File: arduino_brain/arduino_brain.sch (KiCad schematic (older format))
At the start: 57 parts, among them Q1 2N3904, Q10 2N3904, Q11 2N3906, Q2 TIP120, Q3 TIP120, Q4 2N3904, Q5 2N3906, Q6 2N3904, Q7 2N3906, Q8 2N3904, Q9 2N3906, U2 CRE1S2412SC

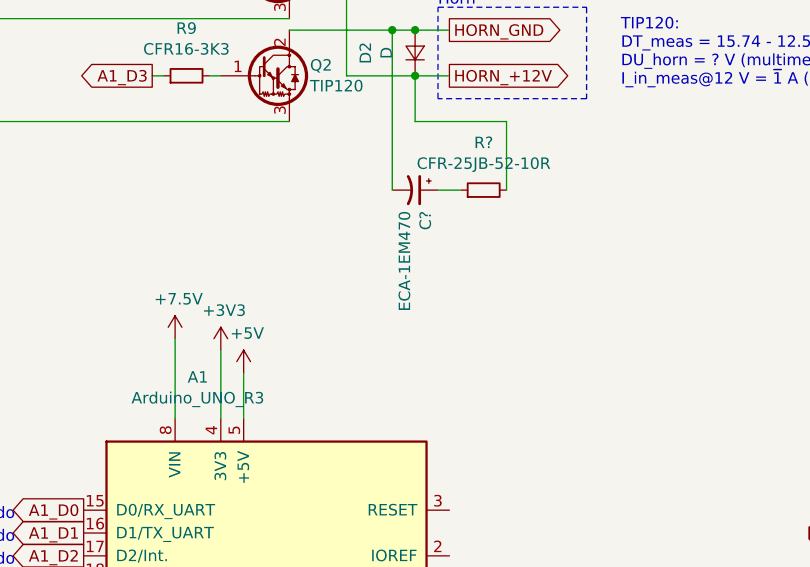
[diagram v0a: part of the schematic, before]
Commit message: Beefed up snubber capacitor
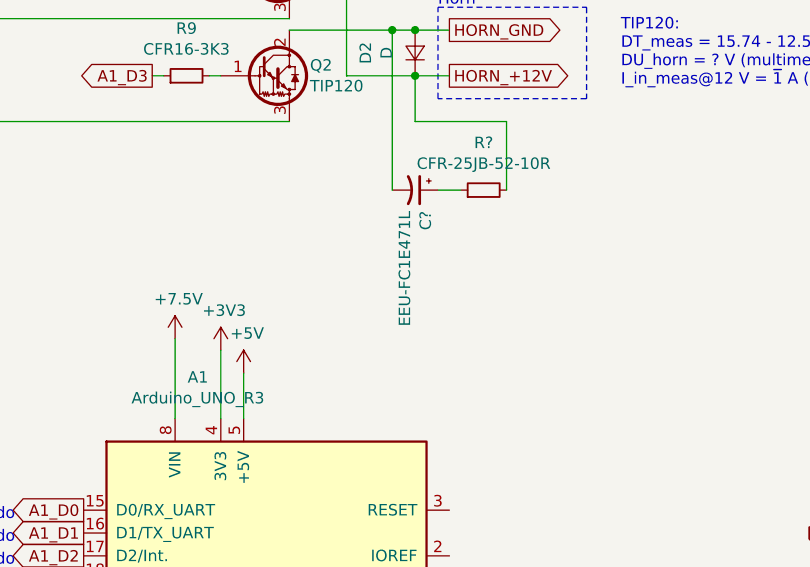
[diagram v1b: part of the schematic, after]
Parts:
- C?: value ECA-1EM470 -> EEU-FC1E471L
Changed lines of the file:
@@
 P 6850 5050
 F 0 "C?" H 6941 5096 50  0000 L CNN
-F 1 "ECA-1EM470" H 6941 5005 50  0000 L CNN
+F 1 "EEU-FC1E471L" H 6941 5005 50  0000 L CNN
 F 2 "" H 6850 5050 50  0001 C CNN
 F 3 "~" H 6850 5050 50  0001 C CNN

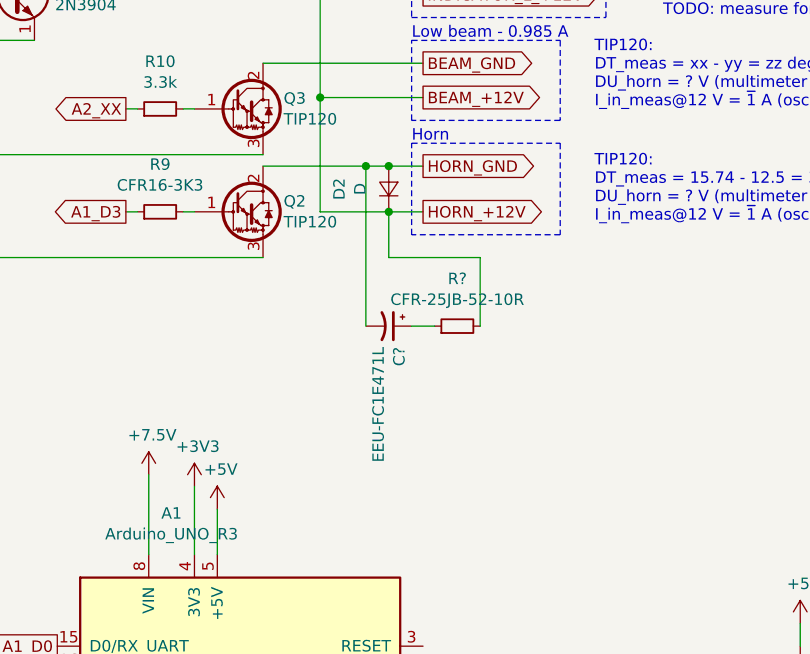
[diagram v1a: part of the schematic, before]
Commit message: Added cap on supply, removed snubber cap
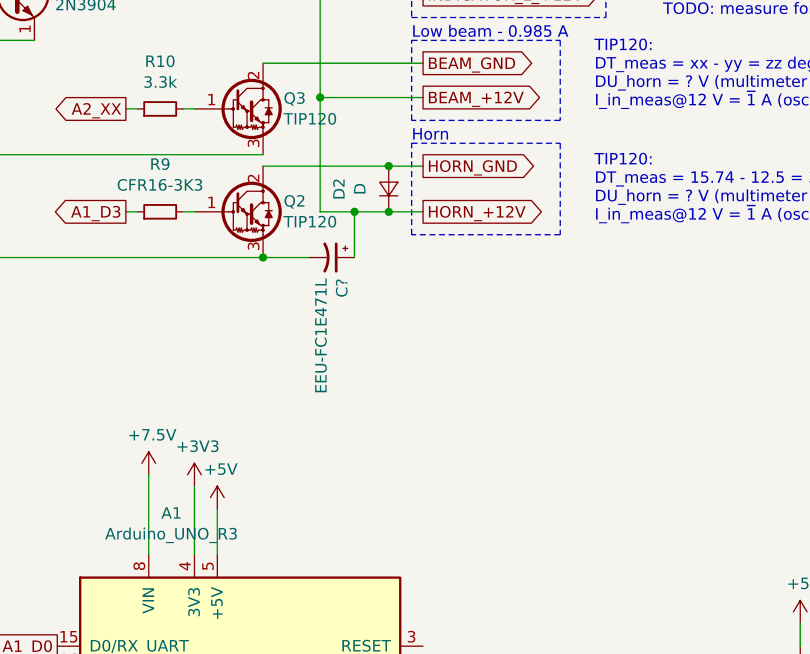
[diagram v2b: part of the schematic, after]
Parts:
- removed R?: CFR-25JB-52-10R, symbol Device:R_Small
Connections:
- net +12V: now also C?.1
- net -BATT: now also C?.2
- net HORN_GND: no longer C?.2
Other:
- moved on the sheet: C?
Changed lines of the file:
@@
 	8650 6350 8650 6450
 Wire Wire Line
-	6550 4550 6850 4550
+	6550 4550 6700 4550
 Wire Wire Line
 	6850 850  6850 2100
 $Comp
-L Device:R_Small R?
-U 1 1 5E512CDD
-P 7150 5050
-F 0 "R?" V 7357 5050 50  0000 C CNN
-F 1 "CFR-25JB-52-10R" V 7266 5050 50  0000 C CNN
-F 2 "" V 7080 5050 50  0001 C CNN
-F 3 "~" H 7150 5050 50  0001 C CNN
-	1    7150 5050
-	0    -1   -1   0
+L Device:CP1_Small C?
+U 1 1 5E54D93D
+P 6600 4750
+F 0 "C?" H 6691 4796 50  0000 L CNN
+F 1 "EEU-FC1E471L" H 6691 4705 50  0000 L CNN
+F 2 "" H 6600 4750 50  0001 C CNN
+F 3 "~" H 6600 4750 50  0001 C CNN
+	1    6600 4750
+	0    1    1    0
 $EndComp
 Wire Wire Line
-	6950 5050 7050 5050
+	6300 4350 6850 4350
 Wire Wire Line
-	6750 5050 6750 4350
+	6500 4750 6300 4750
+Connection ~ 6300 4750
 Wire Wire Line
-	6300 4350 6750 4350
-Connection ~ 6750 4350
+	6700 4750 6700 4550
+Connection ~ 6700 4550
 Wire Wire Line
-	6750 4350 6850 4350
-Wire Wire Line
-	7250 5050 7250 4750
-Wire Wire Line
-	7250 4750 6850 4750
-Wire Wire Line
-	6850 4750 6850 4550
-$Comp
-L Device:CP1_Small C?
-U 1 1 5E54D93D
-P 6850 5050
-F 0 "C?" H 6941 5096 50  0000 L CNN
-F 1 "EEU-FC1E471L" H 6941 5005 50  0000 L CNN
-F 2 "" H 6850 5050 50  0001 C CNN
-F 3 "~" H 6850 5050 50  0001 C CNN
-	1    6850 5050
-	0    1    1    0
-$EndComp
+	6700 4550 6850 4550
 $EndSCHEMATC

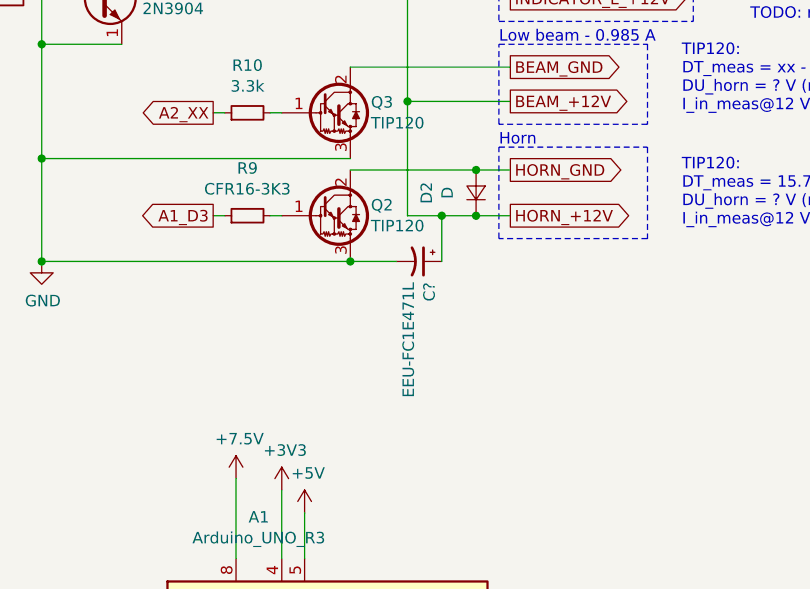
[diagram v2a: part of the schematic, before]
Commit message: Removed cap on supply
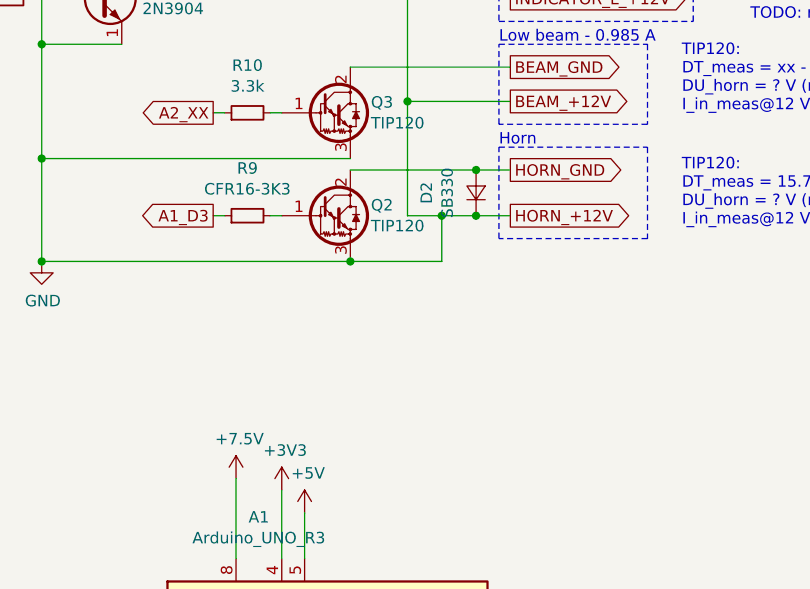
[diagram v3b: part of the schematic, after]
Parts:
- removed C?: EEU-FC1E471L, symbol Device:CP1_Small
- D2: value D -> SB330
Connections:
- net -BATT is gone; now on net +12V: A1.7 (GND), A2.7 (GND), C?.2, C?.2, C?.2, C?.2, C?.2, C?.2, C?.2, C?.2, D?.2 (A), Q10.1 (E), Q2.3 (E), Q3.3 (E), Q4.1 (E), Q6.1 (E), Q6.2 (B), Q8.1 (E), R14.2, R?.1, R?.2, R?.2, U2.1 (-VIN), U2.3 (-VOUT), U?.1 (GND), U?.3 (GND)
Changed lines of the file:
@@
 P 6850 4450
 F 0 "D2" H 6850 4666 50  0000 C CNN
-F 1 "D" H 6850 4575 50  0000 C CNN
+F 1 "SB330" H 6850 4575 50  0000 C CNN
 F 2 "" H 6850 4450 50  0001 C CNN
 F 3 "~" H 6850 4450 50  0001 C CNN
@@
 Wire Wire Line
 	6850 850  6850 2100
-$Comp
-L Device:CP1_Small C?
-U 1 1 5E54D93D
-P 6600 4750
-F 0 "C?" H 6691 4796 50  0000 L CNN
-F 1 "EEU-FC1E471L" H 6691 4705 50  0000 L CNN
-F 2 "" H 6600 4750 50  0001 C CNN
-F 3 "~" H 6600 4750 50  0001 C CNN
-	1    6600 4750
-	0    1    1    0
-$EndComp
 Wire Wire Line
 	6300 4350 6850 4350
-Wire Wire Line
-	6500 4750 6300 4750
 Connection ~ 6300 4750
 Wire Wire Line
@@
 Wire Wire Line
 	6700 4550 6850 4550
+Wire Wire Line
+	6300 4750 6700 4750
 $EndSCHEMATC

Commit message: Added capactitor between base and emitter of pnp transistor horn
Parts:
- added C?: 1C25X7R104K100B, symbol Device:C_Small
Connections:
- net +12V: now also C?.1
- net at Q5.2 (B), R12.2: now also C?.2
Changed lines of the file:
@@
 Wire Wire Line
 	6550 1150 6550 2000
-Wire Wire Line
-	6300 1150 5950 1150
 Connection ~ 6300 1150
 Wire Wire Line
@@
 Wire Wire Line
 	6300 4750 6700 4750
+$Comp
+L Device:C_Small C?
+U 1 1 5E598FF6
+P 6000 1300
+F 0 "C?" V 6229 1300 50  0000 C CNN
+F 1 "1C25X7R104K100B" V 6138 1300 50  0000 C CNN
+F 2 "" H 6000 1300 50  0001 C CNN
+F 3 "~" H 6000 1300 50  0001 C CNN
+	1    6000 1300
+	1    0    0    -1
+$EndComp
+Wire Wire Line
+	5950 1150 6000 1150
+Wire Wire Line
+	6000 1200 6000 1150
+Connection ~ 6000 1150
+Wire Wire Line
+	6000 1150 6300 1150
+Wire Wire Line
+	6000 1400 6000 1450
+Connection ~ 6000 1450
 $EndSCHEMATC

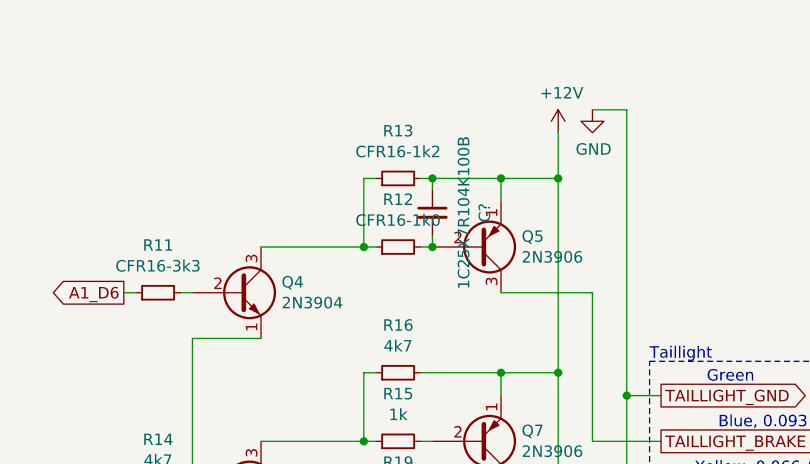
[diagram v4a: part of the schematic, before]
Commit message: Added capactitor in parallel to R2 (EE.SE), removed the previous cap
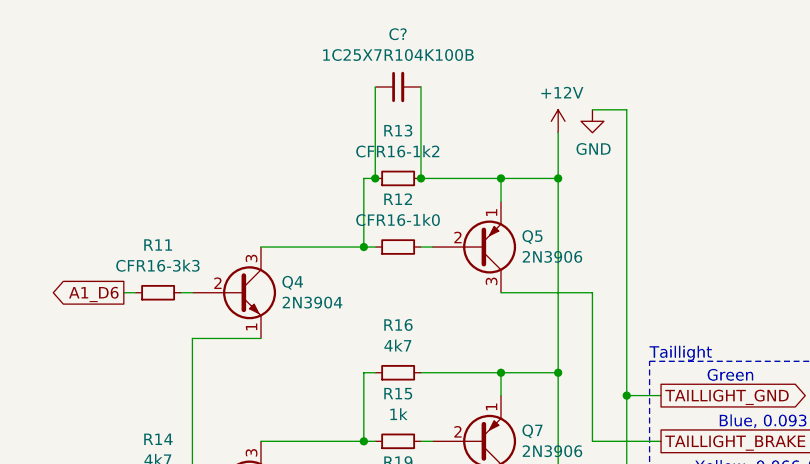
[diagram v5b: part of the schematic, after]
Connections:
- net +12V: now also C?.2; no longer C?.1
- net at Q4.3 (C), R12.1, R13.1: now also C?.1
- net at Q5.2 (B), R12.2: no longer C?.2
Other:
- moved on the sheet: C?
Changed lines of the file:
@@
 L Device:C_Small C?
 U 1 1 5E598FF6
-P 6000 1300
-F 0 "C?" V 6229 1300 50  0000 C CNN
-F 1 "1C25X7R104K100B" V 6138 1300 50  0000 C CNN
-F 2 "" H 6000 1300 50  0001 C CNN
-F 3 "~" H 6000 1300 50  0001 C CNN
-	1    6000 1300
-	1    0    0    -1
+P 5850 750
+F 0 "C?" V 6079 750 50  0000 C CNN
+F 1 "1C25X7R104K100B" V 5988 750 50  0000 C CNN
+F 2 "" H 5850 750 50  0001 C CNN
+F 3 "~" H 5850 750 50  0001 C CNN
+	1    5850 750
+	0    -1   -1   0
 $EndComp
 Wire Wire Line
-	5950 1150 6000 1150
+	5950 750  5950 1150
+Connection ~ 5950 1150
 Wire Wire Line
-	6000 1200 6000 1150
-Connection ~ 6000 1150
+	5750 750  5750 1150
 Wire Wire Line
-	6000 1150 6300 1150
-Wire Wire Line
-	6000 1400 6000 1450
-Connection ~ 6000 1450
+	5950 1150 6300 1150
+Connection ~ 5750 1150
 $EndSCHEMATC

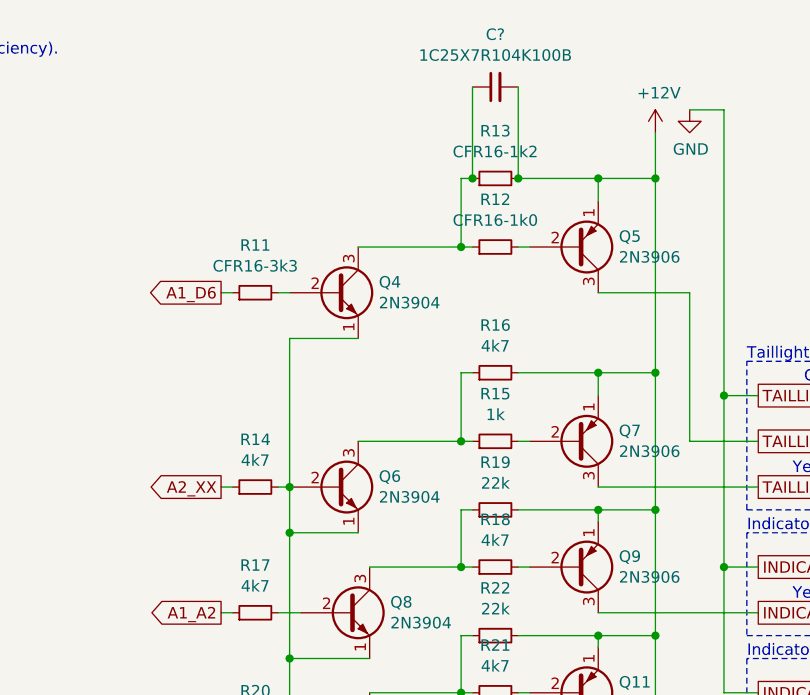
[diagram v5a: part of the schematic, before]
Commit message: Added capactitor between Q3B and Q3E (EE.SE), removed the previous cap
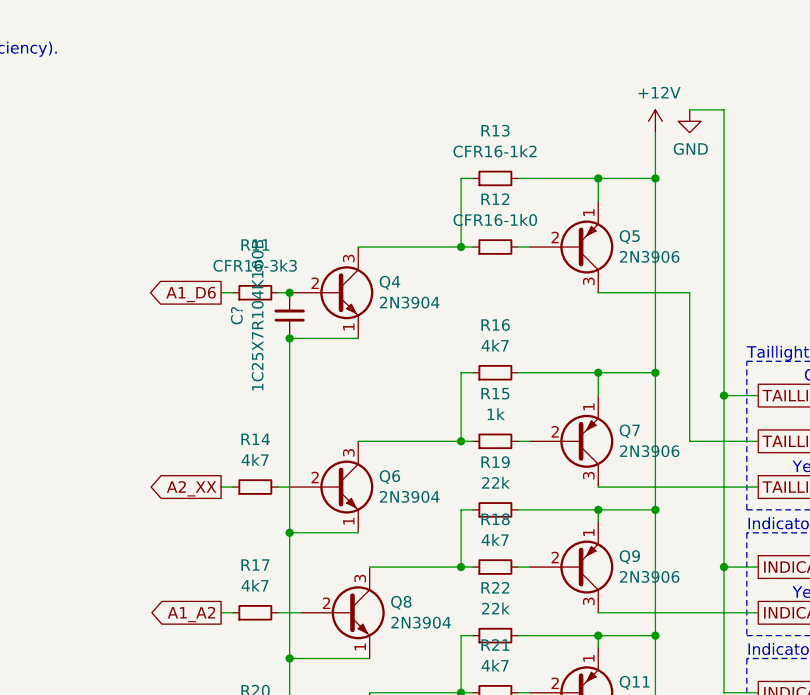
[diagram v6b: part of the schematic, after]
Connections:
- net +12V: now also C?.1; no longer C?.2, Q6.2 (B), R14.2
- net at Q4.2 (B), R11.2: now also C?.2
- net at Q4.3 (C), R12.1, R13.1: no longer C?.1
- new net: Q6.2 (B), R14.2
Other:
- moved on the sheet: C?
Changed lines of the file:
@@
 Wire Wire Line
 	5250 1850 4950 1850
-Wire Wire Line
-	4950 1850 4950 2500
 Connection ~ 4950 2700
-Connection ~ 4950 2500
 Wire Wire Line
 	5250 1450 5700 1450
@@
 Wire Wire Line
 	6850 2100 6850 2850
-Wire Wire Line
-	4950 2500 4950 2700
 Text GLabel 7000 7150 2    50   Output ~ 0
 A1_A1
@@
 L Device:C_Small C?
 U 1 1 5E598FF6
-P 5850 750
-F 0 "C?" V 6079 750 50  0000 C CNN
-F 1 "1C25X7R104K100B" V 5988 750 50  0000 C CNN
-F 2 "" H 5850 750 50  0001 C CNN
-F 3 "~" H 5850 750 50  0001 C CNN
-	1    5850 750
-	0    -1   -1   0
-$EndComp
-Wire Wire Line
-	5950 750  5950 1150
-Connection ~ 5950 1150
-Wire Wire Line
-	5750 750  5750 1150
+P 4950 1750
+F 0 "C?" V 5179 1750 50  0000 C CNN
+F 1 "1C25X7R104K100B" V 5088 1750 50  0000 C CNN
+F 2 "" H 4950 1750 50  0001 C CNN
+F 3 "~" H 4950 1750 50  0001 C CNN
+	1    4950 1750
+	-1   0    0    1
+$EndComp
 Wire Wire Line
 	5950 1150 6300 1150
-Connection ~ 5750 1150
+Wire Wire Line
+	4950 1850 4950 2700
+Connection ~ 4950 1850
+Connection ~ 4950 1650
 $EndSCHEMATC

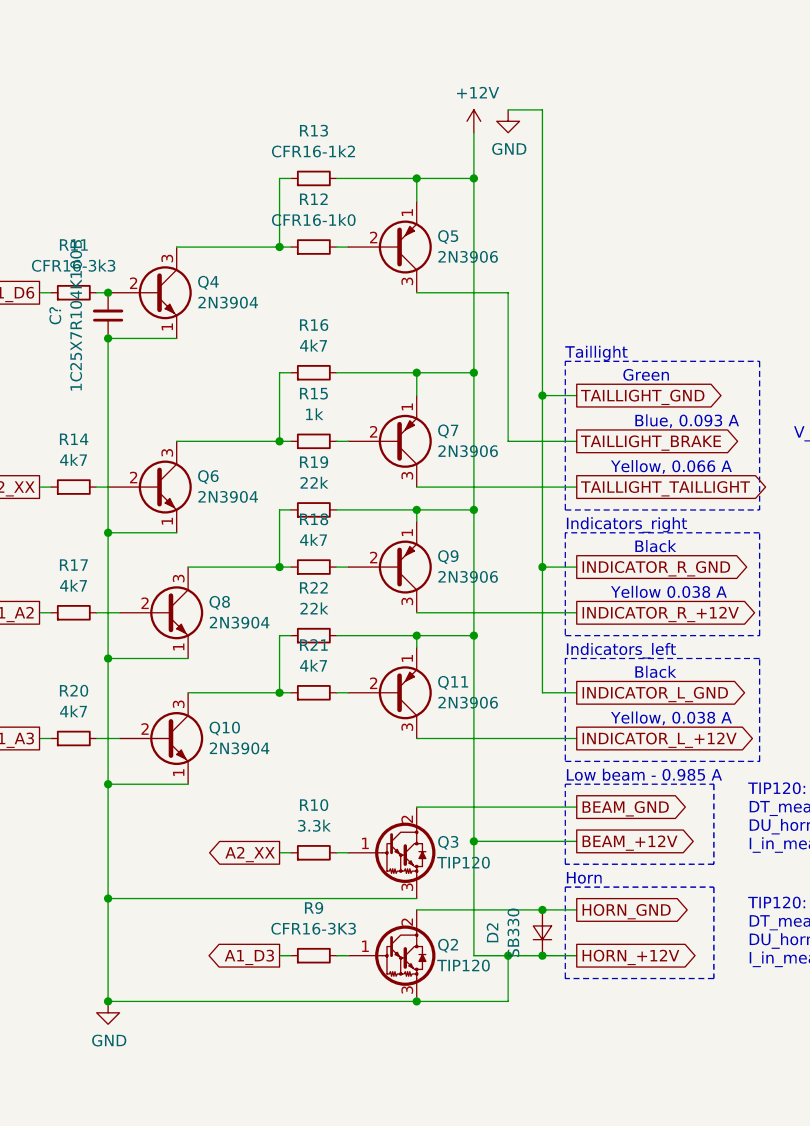
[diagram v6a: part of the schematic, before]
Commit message: Caps between Q4 and Q3 B-C, SB560 replacing SB330
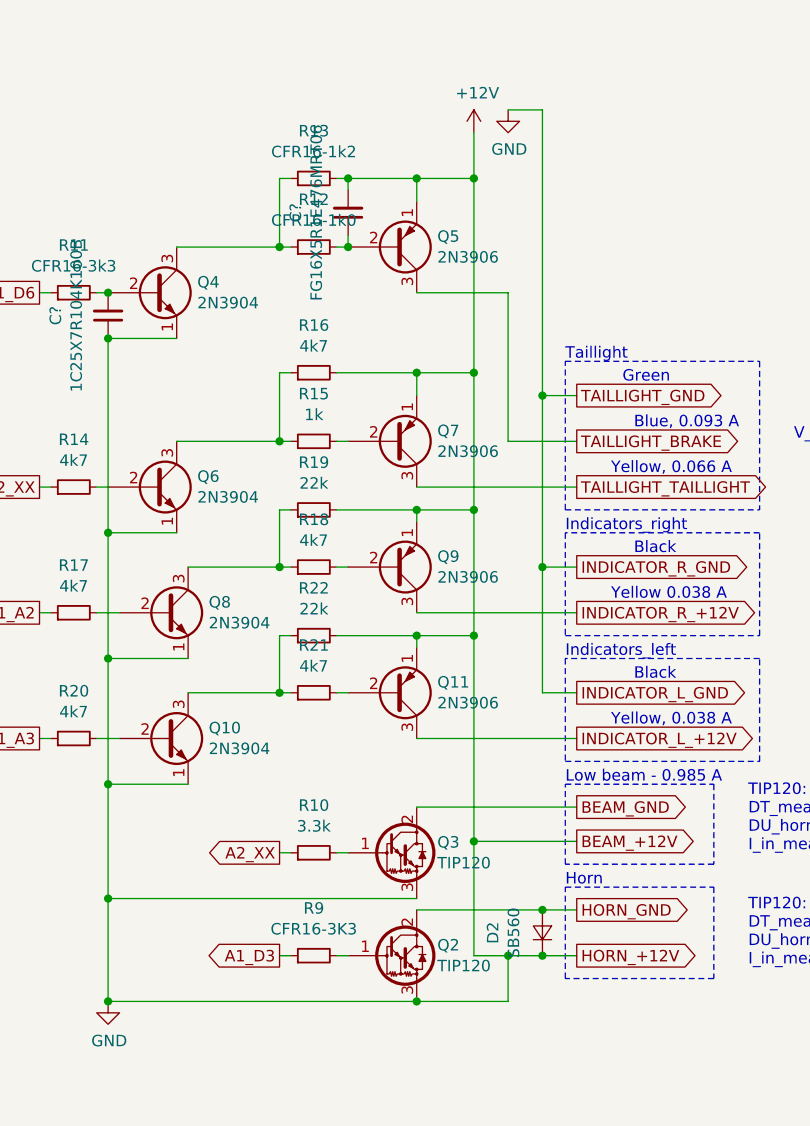
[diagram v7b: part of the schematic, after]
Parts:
- added C?: FG16X5R1E476MRT06, symbol Device:C_Small
- D2: value SB330 -> SB560
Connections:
- net +12V: now also C?.2
- net at Q5.2 (B), R12.2: now also C?.1
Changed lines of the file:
@@
 P 6850 4450
 F 0 "D2" H 6850 4666 50  0000 C CNN
-F 1 "SB330" H 6850 4575 50  0000 C CNN
+F 1 "SB560" H 6850 4575 50  0000 C CNN
 F 2 "" H 6850 4450 50  0001 C CNN
 F 3 "~" H 6850 4450 50  0001 C CNN
@@
 $EndComp
 Wire Wire Line
-	5950 1150 6300 1150
-Wire Wire Line
 	4950 1850 4950 2700
 Connection ~ 4950 1850
 Connection ~ 4950 1650
+$Comp
+L Device:C_Small C?
+U 1 1 5E656B36
+P 6000 1300
+F 0 "C?" V 6229 1300 50  0000 C CNN
+F 1 "FG16X5R1E476MRT06" V 6138 1300 50  0000 C CNN
+F 2 "" H 6000 1300 50  0001 C CNN
+F 3 "~" H 6000 1300 50  0001 C CNN
+	1    6000 1300
+	-1   0    0    1
+$EndComp
+Wire Wire Line
+	6000 1200 6000 1150
+Wire Wire Line
+	5950 1150 6000 1150
+Connection ~ 6000 1150
+Wire Wire Line
+	6000 1150 6300 1150
+Wire Wire Line
+	6000 1400 6000 1450
+Connection ~ 6000 1450
 $EndSCHEMATC

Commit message: Still not working
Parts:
- R9: value CFR16-3K3 -> CFR16-100R
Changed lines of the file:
@@
 P 5850 4550
 F 0 "R9" V 6057 4550 50  0000 C CNN
-F 1 "CFR16-3K3" V 5966 4550 50  0000 C CNN
+F 1 "CFR16-100R" V 5966 4550 50  0000 C CNN
 F 2 "" V 5780 4550 50  0001 C CNN
 F 3 "~" H 5850 4550 50  0001 C CNN
